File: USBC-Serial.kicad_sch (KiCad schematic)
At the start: 10 parts, among them J1 USB_C_Receptacle_USB2.0_16P, J2 Conn_01x06_Pin, U1 CH343P

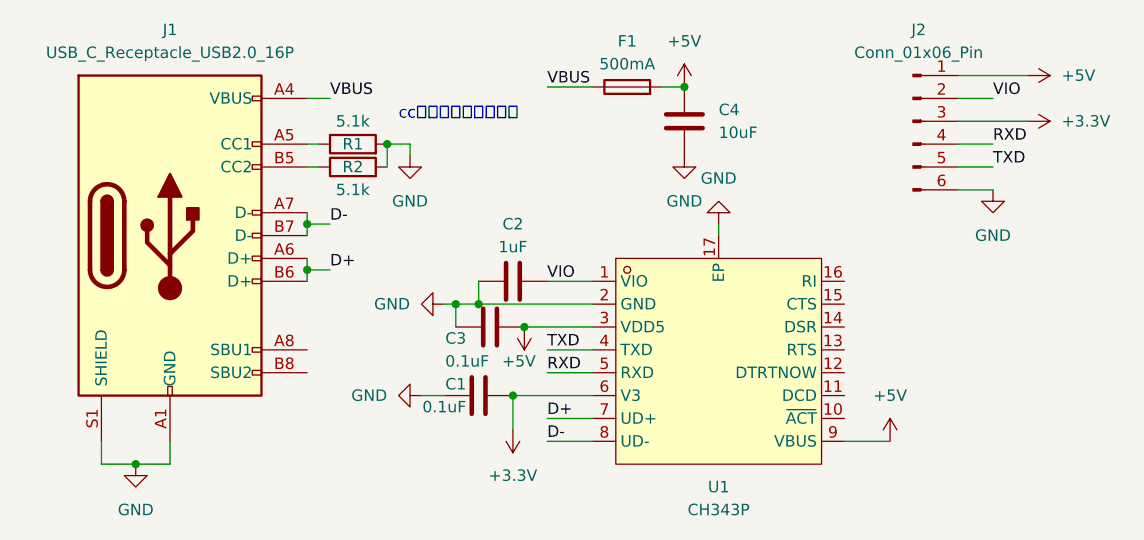
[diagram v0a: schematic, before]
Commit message: remove offensive text
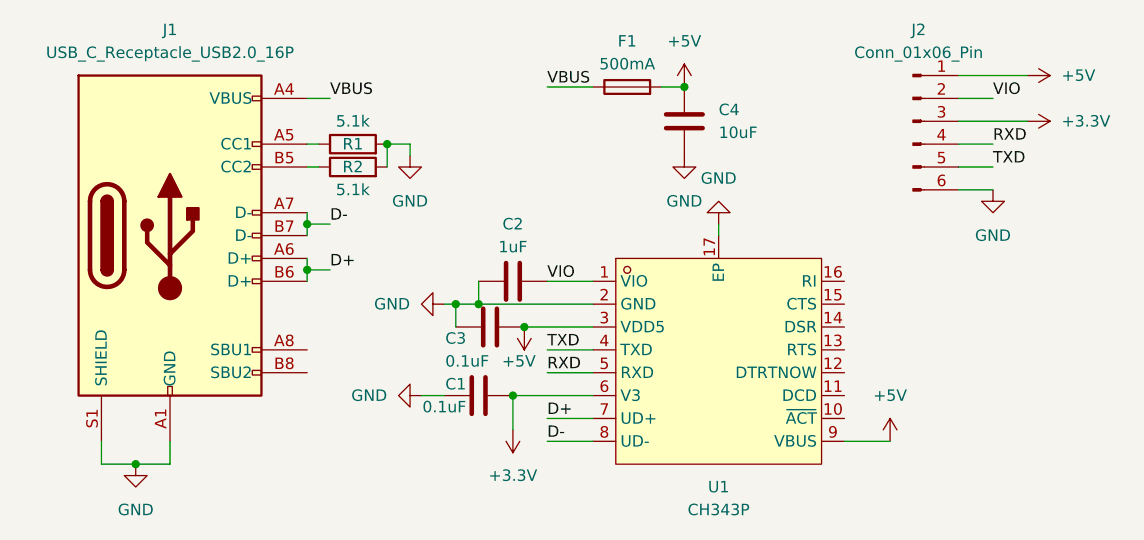
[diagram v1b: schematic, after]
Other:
- note removed: "cc不下拉，全家火葬场"
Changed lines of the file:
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@@
     (stroke (width 0) (type default))
-  )
-  (text "cc不下拉，全家火葬场\n" (at 63.5 35.56 0)
-    (effects (font (size 1.27 1.27)) (justify left bottom))
   )
   (label "RXD" (at 80.01 63.5 0) (fields_autoplaced)
